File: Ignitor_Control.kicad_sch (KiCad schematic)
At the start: 12 parts, among them J20 Ignitor Screw Terminal, K2 G5Q-1A DC24, Q8 BSS138, U8 INA187A1

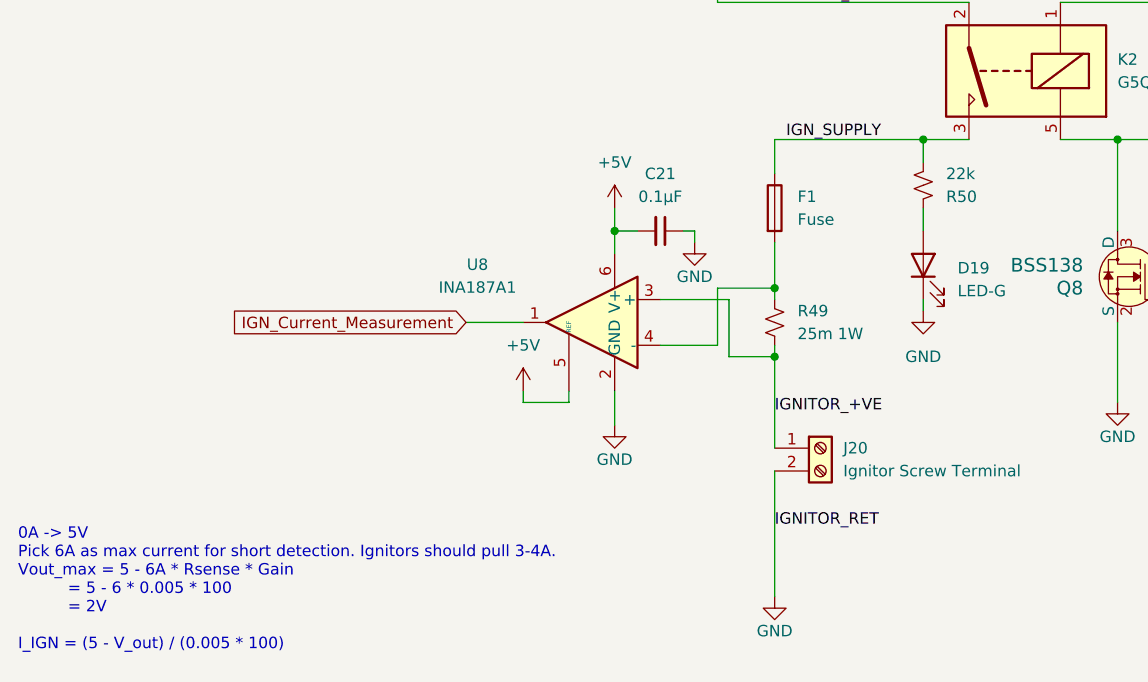
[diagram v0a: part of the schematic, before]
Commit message: minor fixed + lowered status leds to ~0.6mA, which should give ~50 mcd
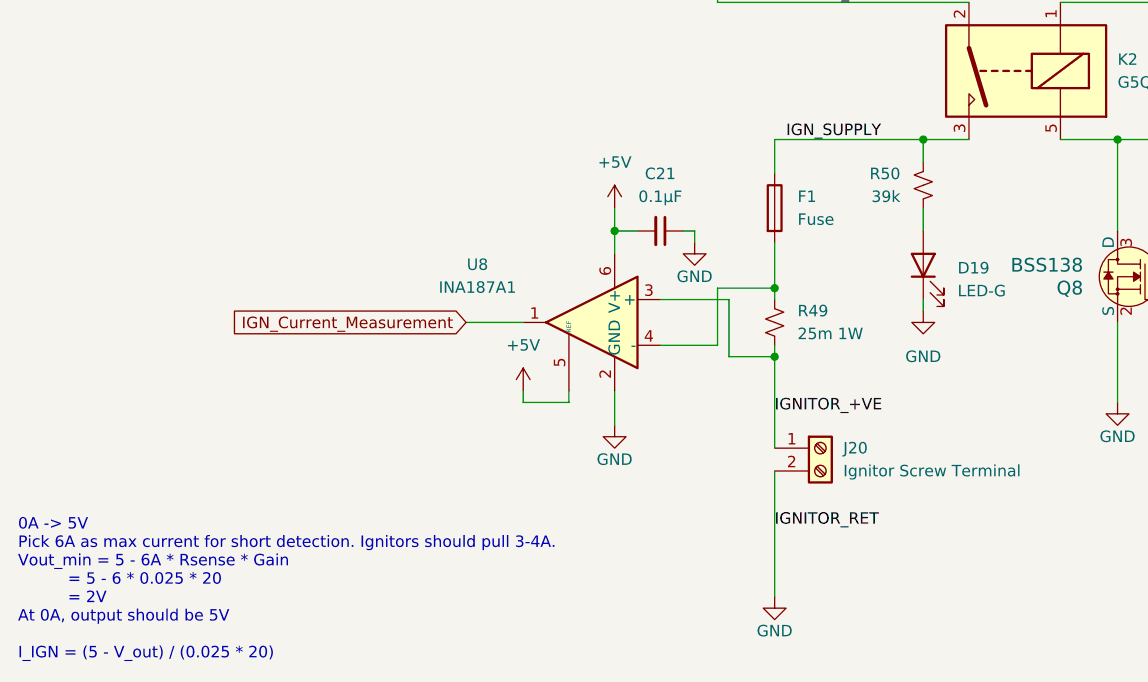
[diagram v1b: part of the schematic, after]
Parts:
- R50: value 22k -> 39k
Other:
- note added: "0A -> 5V Pick 6A as max current for short detection. Ignitors should pull 3-4A. Vout_min = 5 - 6A * Rsense * Gain = 5 - 6 * 0.025 * 20 = 2V At 0A, output should be 5V I_IGN = (5 - V_out) / (0.025 * 20)"
- note removed: "0A -> 5V Pick 6A as max current for short detection. Ignitors should pull 3-4A. Vout_max = 5 - 6A * Rsense * Gain = 5 - 6 * 0.005 * 100 = 2V I_IGN = (5 - V_out) / (0.005 * 100)"
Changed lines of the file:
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@@
 		(company "Queen's Rocket Engineering Team")
 	)
-	(text "0A -> 5V\nPick 6A as max current for short detection. Ignitors should pull 3-4A.\nVout_max = 5 - 6A * Rsense * Gain\n          = 5 - 6 * 0.005 * 100\n          = 2V\n\nI_IGN = (5 - V_out) / (0.005 * 100)"
+	(text "0A -> 5V\nPick 6A as max current for short detection. Ignitors should pull 3-4A.\nVout_min = 5 - 6A * Rsense * Gain\n          = 5 - 6 * 0.025 * 20\n          = 2V\nAt 0A, output should be 5V\n\nI_IGN = (5 - V_out) / (0.025 * 20)"
 		(exclude_from_sim no)
 		(at 78.486 138.938 0)
@@
 		(fields_autoplaced yes)
 		(property "Reference" "R50"
-			(at 181.61 95.2501 0)
-			(effects
-				(font
-					(size 1.27 1.27)
-				)
-				(justify left)
-			)
-		)
-		(property "Value" "22k"
-			(at 181.61 92.7101 0)
-			(effects
-				(font
-					(size 1.27 1.27)
-				)
-				(justify left)
-			)
-		)
+			(at 176.53 92.7099 0)
+			(effects
+				(font
+					(size 1.27 1.27)
+				)
+				(justify right)
+			)
+		)
+		(property "Value" "39k"
+			(at 176.53 95.2499 0)
+			(effects
+				(font
+					(size 1.27 1.27)
+				)
+				(justify right)
+			)
+		)

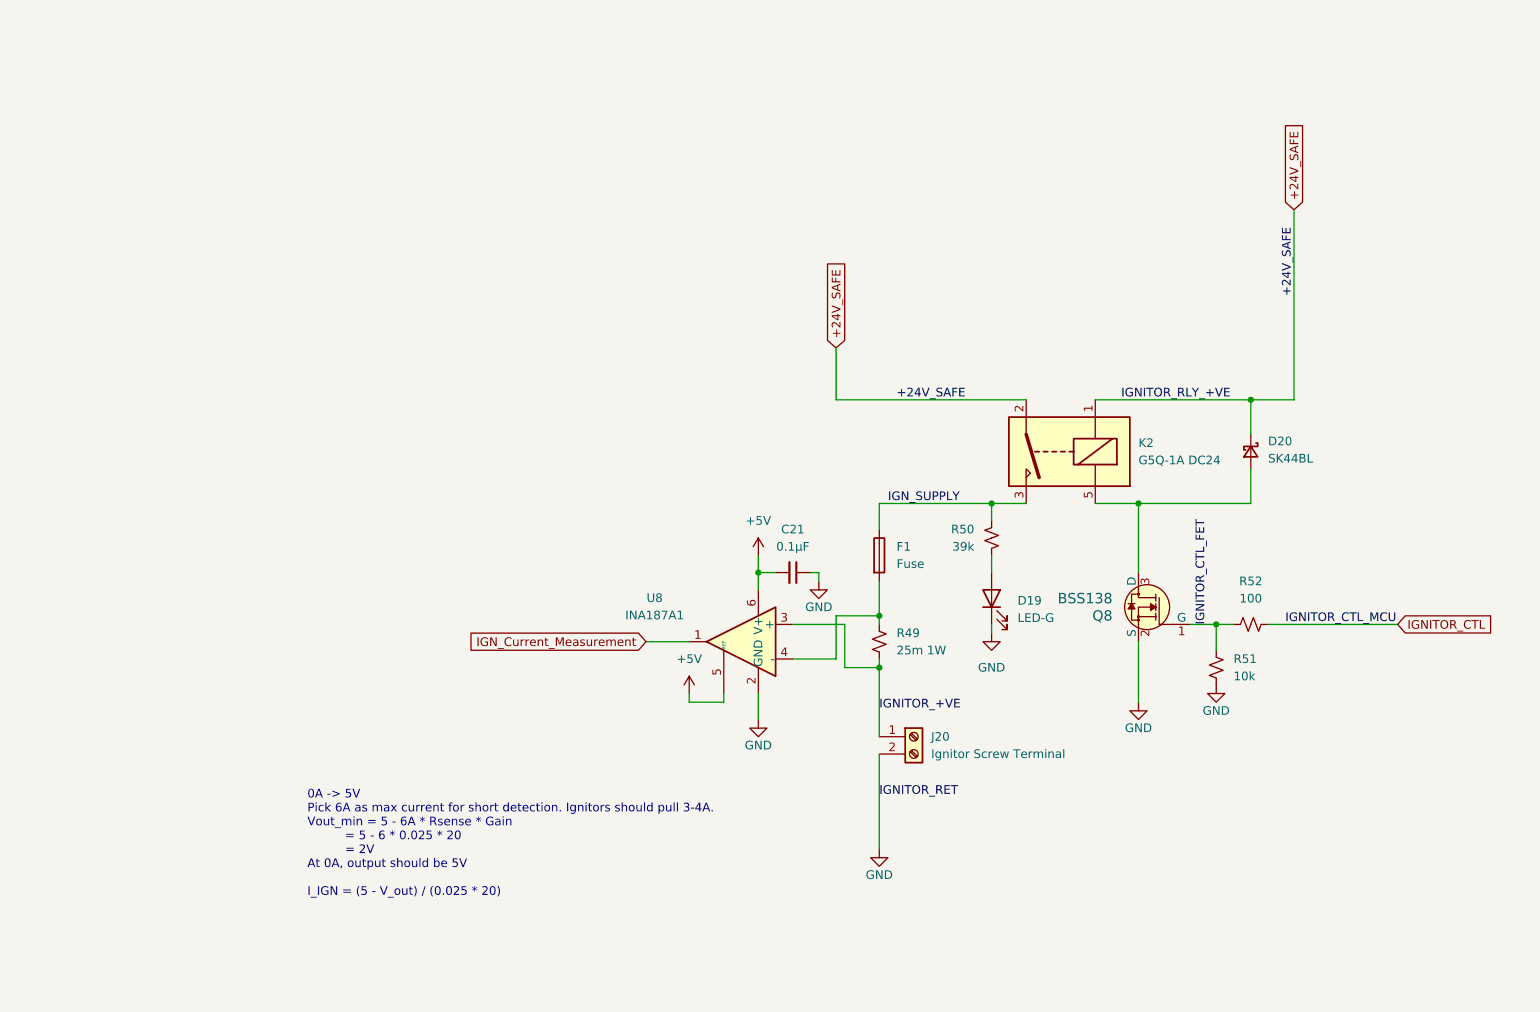
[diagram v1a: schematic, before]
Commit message: revamped schematic to be more readable
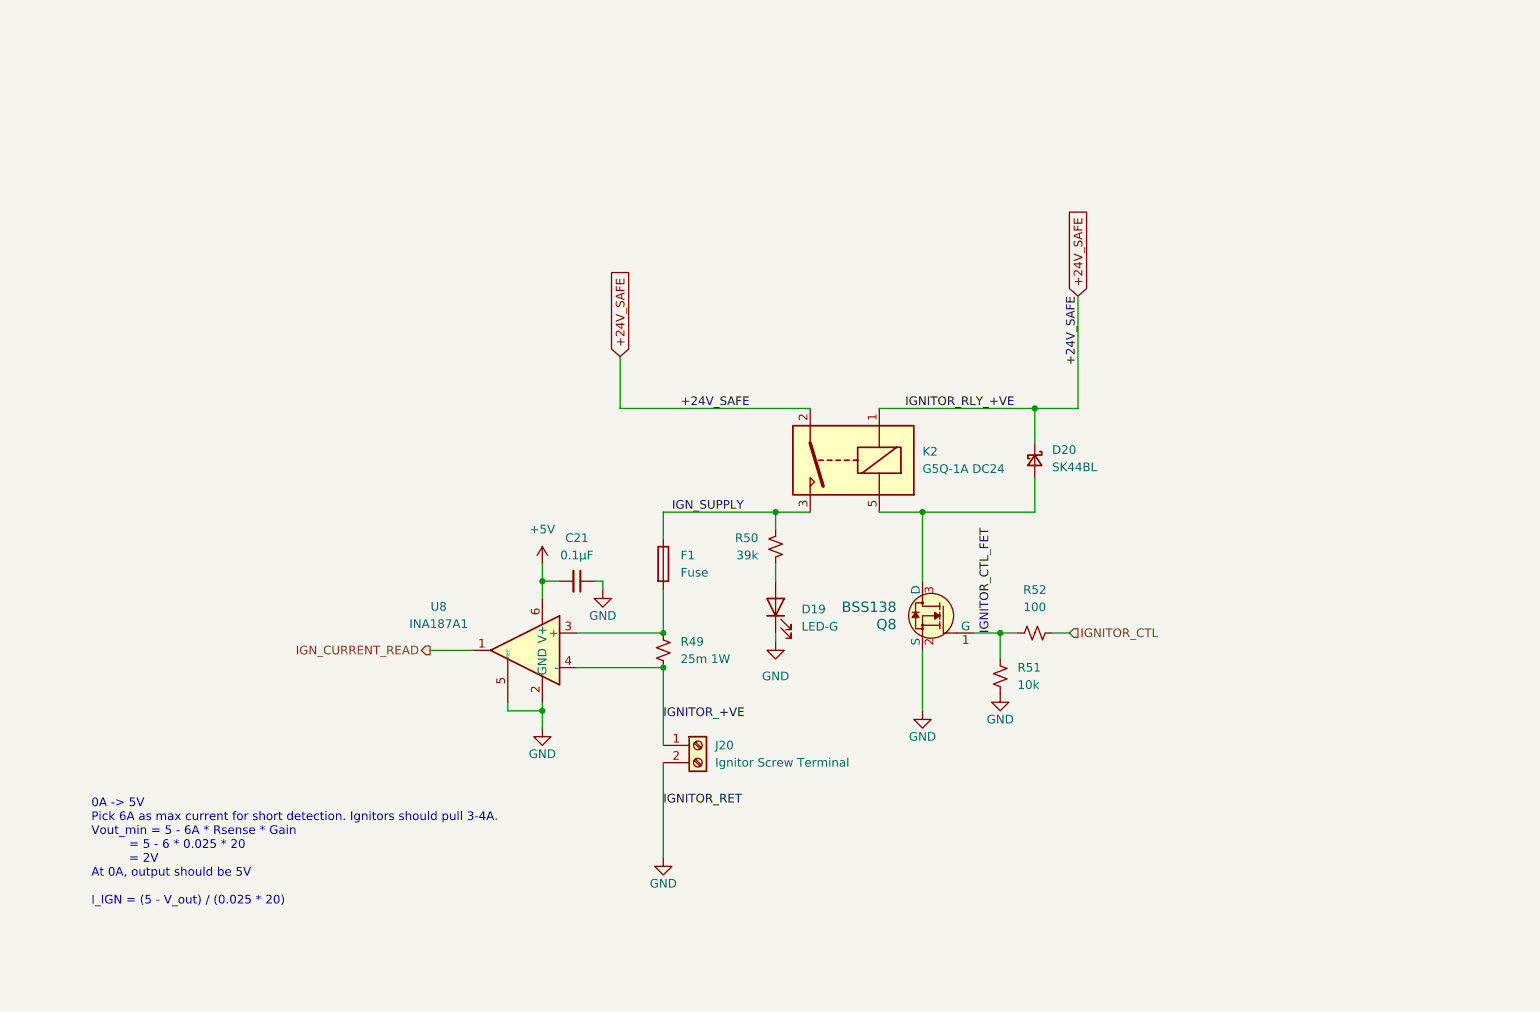
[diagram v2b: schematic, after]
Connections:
- net +5V: no longer U8.5 (REF)
- net GND: now also U8.5 (REF)
- net IGNITOR_+VE: now also U8.4 (-); no longer U8.3 (+)
- net at F1.2, R49.1: now also U8.3 (+); no longer U8.4 (-)
- net IGN_Current_Measurement renamed IGN_CURRENT_READ
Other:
- moved on the sheet: C21, D19, D20, F1, J20, K2, Q8, R49, R50, R51, R52, U8

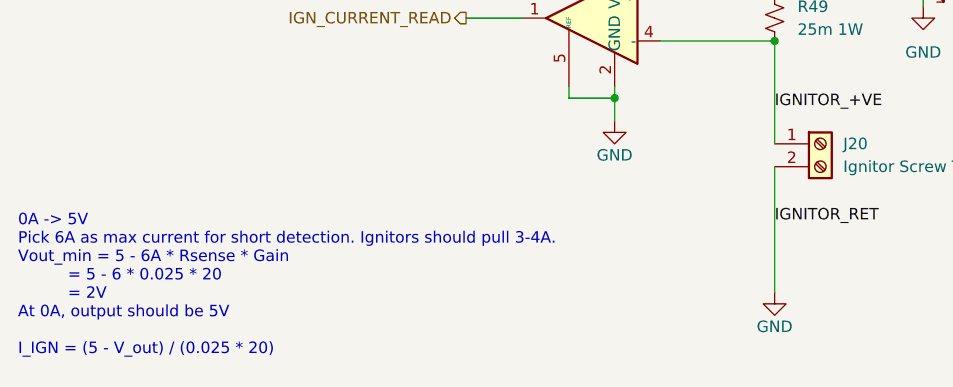
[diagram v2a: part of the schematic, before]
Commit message: add power sequencing
add usb VBUS ORing
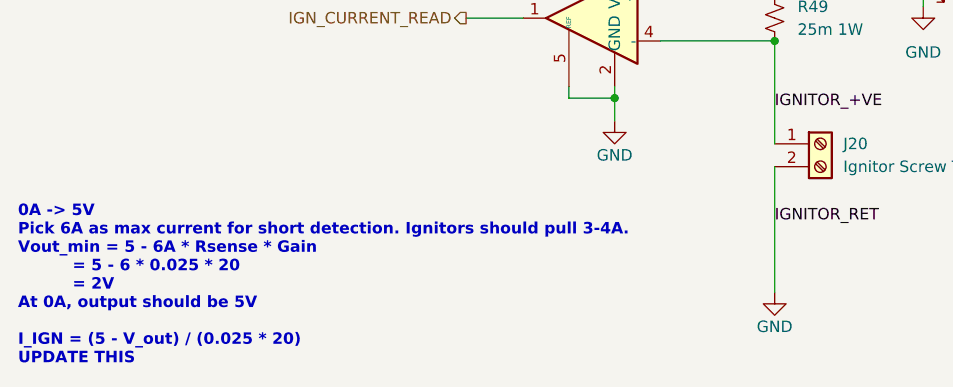
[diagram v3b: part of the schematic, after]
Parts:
- U8: LCSC (none) -> C49262296
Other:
- note added: "0A -> 5V Pick 6A as max current for short detection. Ignitors should pull 3-4A. Vout_min = 5 - 6A * Rsense * Gain = 5 - 6 * 0.025 * 20 = 2V At 0A, output should be 5V I_IGN = (5 - V_out) / (0.025 * 20) UPDATE THIS"
- note removed: "0A -> 5V Pick 6A as max current for short detection. Ignitors should pull 3-4A. Vout_min = 5 - 6A * Rsense * Gain = 5 - 6 * 0.025 * 20 = 2V At 0A, output should be 5V I_IGN = (5 - V_out) / (0.025 * 20)"
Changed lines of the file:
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@@
 		(company "Queen's Rocket Engineering Team")
 	)
-	(text "0A -> 5V\nPick 6A as max current for short detection. Ignitors should pull 3-4A.\nVout_min = 5 - 6A * Rsense * Gain\n          = 5 - 6 * 0.025 * 20\n          = 2V\nAt 0A, output should be 5V\n\nI_IGN = (5 - V_out) / (0.025 * 20)"
+	(text "0A -> 5V\nPick 6A as max current for short detection. Ignitors should pull 3-4A.\nVout_min = 5 - 6A * Rsense * Gain\n          = 5 - 6 * 0.025 * 20\n          = 2V\nAt 0A, output should be 5V\n\nI_IGN = (5 - V_out) / (0.025 * 20)\nUPDATE THIS"
 		(exclude_from_sim no)
 		(at 46.736 140.208 0)
@@
 			(font
 				(size 1.27 1.27)
+				(thickness 0.254)
+				(bold yes)
 			)
 			(justify left)
@@
 			(at 110.49 110.49 0)
 			(effects
+				(font
+					(size 1.27 1.27)
+				)
+				(hide yes)
+			)
+		)
+		(property "LCSC" "C49262296"
+			(at 110.49 110.49 0)
+			(effects

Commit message: minor fixes
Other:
- moved on the sheet: J20, R51
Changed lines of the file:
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@@
 	(wire
 		(pts
-			(xy 168.91 110.49) (xy 168.91 119.38)
+			(xy 168.91 110.49) (xy 168.91 111.76)
 		)
 		(stroke
@@
 	(wire
 		(pts
-			(xy 124.46 74.93) (xy 124.46 67.31)
-		)
-		(stroke
-			(width 0)
-			(type default)
-		)
-	)
-	(wire
-		(pts
 			(xy 120.65 100.33) (xy 121.92 100.33)
 		)
@@
 	(wire
 		(pts
-			(xy 130.81 113.03) (xy 130.81 124.46)
+			(xy 130.81 113.03) (xy 130.81 121.92)
 		)
 		(stroke
@@
 	(wire
 		(pts
-			(xy 191.77 74.93) (xy 185.42 74.93)
-		)
-		(stroke
-			(width 0)
-			(type default)
-		)
-	)
-	(wire
-		(pts
 			(xy 168.91 90.17) (xy 168.91 100.33)
 		)
@@
 	(wire
 		(pts
-			(xy 191.77 58.42) (xy 191.77 74.93)
+			(xy 185.42 73.66) (xy 185.42 74.93)
 		)
 		(stroke
@@
 	(wire
 		(pts
-			(xy 96.52 110.49) (xy 102.87 110.49)
-		)
-		(stroke
-			(width 0)
-			(type default)
-		)
-	)
-	(wire
-		(pts
-			(xy 124.46 74.93) (xy 152.4 74.93)
+			(xy 99.06 110.49) (xy 102.87 110.49)
 		)
 		(stroke
@@
 	(wire
 		(pts
-			(xy 180.34 107.95) (xy 180.34 111.76)
+			(xy 180.34 107.95) (xy 180.34 109.22)
 		)
 		(stroke
@@
 	(wire
 		(pts
+			(xy 152.4 73.66) (xy 152.4 74.93)
+		)
+		(stroke
+			(width 0)
+			(type default)
+		)
+	)
+	(wire
+		(pts
 			(xy 162.56 74.93) (xy 185.42 74.93)
 		)
@@
 	(wire
 		(pts
-			(xy 130.81 127) (xy 130.81 140.97)
+			(xy 130.81 124.46) (xy 130.81 132.08)
 		)
 		(stroke
@@
 		(pts
 			(xy 162.56 90.17) (xy 168.91 90.17)
+		)
+		(stroke
+			(width 0)
+			(type default)
+		)
+	)
+	(wire
+		(pts
+			(xy 180.34 115.57) (xy 180.34 114.3)
 		)
 		(stroke
@@
 	)
 	(label "IGNITOR_+VE"
-		(at 130.81 120.65 0)
+		(at 130.81 116.84 0)
 		(effects
 			(font
@@
 			)
 			(justify left bottom)
-		)
-	)
-	(label "+24V_SAFE"
-		(at 191.77 58.42 270)
-		(effects
-			(font
-				(size 1.27 1.27)
-			)
-			(justify right bottom)
 		)
 	)
@@
 		)
 	)
-	(label "+24V_SAFE"
-		(at 133.35 74.93 0)
+	(label "IGNITOR_RET"
+		(at 130.81 130.81 0)
 		(effects
 			(font
@@
 		)
 	)
-	(label "IGNITOR_RET"
-		(at 130.81 133.35 0)
-		(effects
-			(font
-				(size 1.27 1.27)
-			)
-			(justify left bottom)
-		)
-	)
 	(global_label "+24V_SAFE"
 		(shape input)
-		(at 191.77 58.42 90)
+		(at 185.42 73.66 90)
 		(fields_autoplaced yes)
 		(effects
@@
 		)
 		(property "Intersheetrefs" "${INTERSHEET_REFS}"
-			(at 191.77 44.8515 90)
+			(at 185.42 60.0915 90)
 			(effects
 				(font
@@
 	(global_label "+24V_SAFE"
 		(shape input)
-		(at 124.46 67.31 90)
+		(at 152.4 73.66 90)
 		(fields_autoplaced yes)
 		(effects
@@
 		)
 		(property "Intersheetrefs" "${INTERSHEET_REFS}"
-			(at 124.46 53.7415 90)
+			(at 152.4 60.0915 90)
 			(effects
 				(font
@@
 	(hierarchical_label "IGN_CURRENT_READ"
 		(shape output)
-		(at 96.52 110.49 180)
+		(at 99.06 110.49 180)
 		(effects
 			(font
@@
 	(symbol
 		(lib_id "power:GND")
-		(at 130.81 140.97 0)
+		(at 130.81 132.08 0)
 		(unit 1)
 		(exclude_from_sim no)
@@
 		(dnp no)
 		(property "Reference" "#PWR0120"
-			(at 130.81 147.32 0)
+			(at 130.81 138.43 0)
 			(effects
 				(font
@@
 		)
 		(property "Value" "GND"
-			(at 130.81 144.78 0)
+			(at 130.81 135.89 0)
 			(effects
 				(font
@@
 		)
 		(property "Footprint" ""
-			(at 130.81 140.97 0)
+			(at 130.81 132.08 0)
 			(effects
 				(font
@@
 		)
 		(property "Datasheet" ""
-			(at 130.81 140.97 0)
+			(at 130.81 132.08 0)
 			(effects
 				(font
@@
 		)
 		(property "Description" "Power symbol creates a global label with name \"GND\" , ground"
-			(at 130.81 140.97 0)
+			(at 130.81 132.08 0)
 			(effects
 				(font
@@
 		(dnp no)
 		(property "Reference" "U8"
-			(at 97.79 104.0698 0)
+			(at 105.156 103.378 0)
 			(effects
 				(font
@@
 		)
 		(property "Value" "INA187A1"
-			(at 97.79 106.6098 0)
+			(at 105.156 105.918 0)
 			(effects
 				(font
@@
 	(symbol
 		(lib_id "power:GND")
-		(at 168.91 119.38 0)
+		(at 168.91 111.76 0)
 		(unit 1)
 		(exclude_from_sim no)
@@
 		(dnp no)
 		(property "Reference" "#PWR0122"
-			(at 168.91 125.73 0)
+			(at 168.91 118.11 0)
 			(effects
 				(font
@@
 		)
 		(property "Value" "GND"
-			(at 168.91 123.19 0)
+			(at 168.91 115.57 0)
 			(effects
 				(font
@@
 		)
 		(property "Footprint" ""
-			(at 168.91 119.38 0)
+			(at 168.91 111.76 0)
 			(effects
 				(font
@@
 		)
 		(property "Datasheet" ""
-			(at 168.91 119.38 0)
+			(at 168.91 111.76 0)
 			(effects
 				(font
@@
 		)
 		(property "Description" "Power symbol creates a global label with name \"GND\" , ground"
-			(at 168.91 119.38 0)
+			(at 168.91 111.76 0)
 			(effects
 				(font
@@
 	(symbol
 		(lib_id "Connector:Screw_Terminal_01x02")
-		(at 135.89 124.46 0)
+		(at 135.89 121.92 0)
 		(unit 1)
 		(exclude_from_sim no)
@@
 		(fields_autoplaced yes)
 		(property "Reference" "J20"
+			(at 138.43 121.9199 0)
+			(effects
+				(font
+					(size 1.27 1.27)
+				)
+				(justify left)
+			)
+		)
+		(property "Value" "Ignitor Screw Terminal"
 			(at 138.43 124.4599 0)
 			(effects
@@
 			)
 		)
-		(property "Value" "Ignitor Screw Terminal"
-			(at 138.43 126.9999 0)
-			(effects
-				(font
-					(size 1.27 1.27)
-				)
-				(justify left)
-			)
-		)
 		(property "Footprint" "TerminalBlock_4Ucon:TerminalBlock_4Ucon_1x02_P3.50mm_Vertical"
-			(at 135.89 124.46 0)
+			(at 135.89 121.92 0)
 			(effects
 				(font
@@
 		)
 		(property "Datasheet" "~"
-			(at 135.89 124.46 0)
+			(at 135.89 121.92 0)
 			(effects
 				(font
@@
 		)
 		(property "Description" "Generic screw terminal, single row, 01x02, script generated (kicad-library-utils/schlib/autogen/connector/)"
-			(at 135.89 124.46 0)
+			(at 135.89 121.92 0)
 			(effects
 				(font
@@
 		)
 		(property "Digikey Link" "https://www.digikey.ca/en/products/detail/on-shore-technology-inc/OSTTE020104/2351816"
-			(at 135.89 124.46 0)
+			(at 135.89 121.92 0)
 			(effects
 				(font
@@
 		)
 		(property "Digikey PN" "ED2740-ND"
-			(at 135.89 124.46 0)
+			(at 135.89 121.92 0)
 			(effects
 				(font
@@
 		)
 		(property "MPN" "OSTTE020104"
-			(at 135.89 124.46 0)
+			(at 135.89 121.92 0)
 			(effects
 				(font
@@
 	(symbol
 		(lib_id "Device:R_Small_US")
-		(at 180.34 114.3 0)
+		(at 180.34 111.76 0)
 		(unit 1)
 		(exclude_from_sim no)
@@
 		(on_board yes)
 		(dnp no)
-		(fields_autoplaced yes)
 		(property "Reference" "R51"
-			(at 182.88 113.0299 0)
+			(at 175.26 111.252 0)
 			(effects
 				(font
@@
 		)
 		(property "Value" "10k"
-			(at 182.88 115.5699 0)
+			(at 175.26 113.792 0)
 			(effects
 				(font
@@
 		)
 		(property "Footprint" "Resistor_SMD:R_0402_1005Metric"
-			(at 180.34 114.3 0)
+			(at 180.34 111.76 0)
 			(effects
 				(font
@@
 		)
 		(property "Datasheet" "~"
-			(at 180.34 114.3 0)
+			(at 180.34 111.76 0)
 			(effects
 				(font
@@
 		)
 		(property "Description" "Resistor, small US symbol"
-			(at 180.34 114.3 0)
+			(at 180.34 111.76 0)
 			(effects
 				(font
@@
 		)
 		(property "LCSC" "C25531"
-			(at 180.34 114.3 0)
+			(at 180.34 111.76 0)
 			(effects
 				(font
@@
 		)
 		(property "MPN" "0402WGJ0103TCE"
-			(at 180.34 114.3 0)
+			(at 180.34 111.76 0)
 			(effects
 				(font
@@
 	(symbol
 		(lib_id "power:GND")
-		(at 180.34 116.84 0)
+		(at 180.34 115.57 0)
 		(unit 1)
 		(exclude_from_sim no)
@@
 		(dnp no)
 		(property "Reference" "#PWR0123"
-			(at 180.34 123.19 0)
+			(at 180.34 121.92 0)
 			(effects
 				(font
@@
 		)
 		(property "Value" "GND"
-			(at 180.34 120.65 0)
+			(at 180.34 119.38 0)
 			(effects
 				(font
@@
 		)
 		(property "Footprint" ""
-			(at 180.34 116.84 0)
+			(at 180.34 115.57 0)
 			(effects
 				(font
@@
 		)
 		(property "Datasheet" ""
-			(at 180.34 116.84 0)
+			(at 180.34 115.57 0)
 			(effects
 				(font
@@
 		)
 		(property "Description" "Power symbol creates a global label with name \"GND\" , ground"
-			(at 180.34 116.84 0)
+			(at 180.34 115.57 0)
 			(effects
 				(font
@@
 		(on_board yes)
 		(dnp no)
-		(fields_autoplaced yes)
 		(property "Reference" "R52"
-			(at 185.42 101.6 90)
+			(at 185.166 102.362 90)
 			(effects
 				(font
@@
 		)
 		(property "Value" "100"
-			(at 185.42 104.14 90)
-			(effects
-				(font
+			(at 185.166 104.902 90)
+			(effects
+				(font
